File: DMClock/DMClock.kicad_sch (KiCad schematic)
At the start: 4 parts, among them J5 Conn_01x07_Pin, J6 Conn_01x07_Pin, J7 Conn_01x07_Pin, J8 Conn_01x07_Pin

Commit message: update second layer finalizations
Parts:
- removed J7, J8: Conn_01x07_Pin, Connector_PinSocket_2.54mm:PinSocket_1x07_P2.54mm_Vertical, symbol Connector:Conn_01x07_Pin
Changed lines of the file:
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@@
   (junction (at 123.6883 77.597) (diameter 0) (color 0 0 0 0)
   )
-  (junction (at 108.1415 41.402) (diameter 0) (color 0 0 0 0)
-  )
-  (junction (at 108.1415 33.782) (diameter 0) (color 0 0 0 0)
-  )
   (junction (at 109.474 61.087) (diameter 0) (color 0 0 0 0)
   )
-  (junction (at 108.1415 26.162) (diameter 0) (color 0 0 0 0)
-  )
   (junction (at 119.6963 33.782) (diameter 0) (color 0 0 0 0)
   )
-  (junction (at 108.1415 31.242) (diameter 0) (color 0 0 0 0)
-  )
   (junction (at 123.317 81.407) (diameter 0) (color 0 0 0 0)
   )
   (junction (at 119.6963 41.402) (diameter 0) (color 0 0 0 0)
   )
-  (junction (at 111.8702 28.702) (diameter 0) (color 0 0 0 0)
-  )
-  (junction (at 111.8702 31.242) (diameter 0) (color 0 0 0 0)
-  )
-  (junction (at 111.8702 36.322) (diameter 0) (color 0 0 0 0)
-  )
   (junction (at 125.349 79.502) (diameter 0) (color 0 0 0 0)
   )
   (junction (at 119.6963 26.162) (diameter 0) (color 0 0 0 0)
   )
-  (junction (at 108.1415 36.322) (diameter 0) (color 0 0 0 0)
-  )
-  (junction (at 111.8702 41.402) (diameter 0) (color 0 0 0 0)
-  )
   (junction (at 119.6963 28.702) (diameter 0) (color 0 0 0 0)
   )
   (junction (at 119.6963 38.862) (diameter 0) (color 0 0 0 0)
   )
-  (junction (at 108.1415 38.862) (diameter 0) (color 0 0 0 0)
-  )
   (junction (at 119.6963 31.242) (diameter 0) (color 0 0 0 0)
   )
   (junction (at 99.695 54.737) (diameter 0) (color 0 0 0 0)
   )
-  (junction (at 111.8702 33.782) (diameter 0) (color 0 0 0 0)
-  )
-  (junction (at 108.1415 28.702) (diameter 0) (color 0 0 0 0)
-  )
-  (junction (at 111.8702 26.162) (diameter 0) (color 0 0 0 0)
-  )
-  (junction (at 111.8702 38.862) (diameter 0) (color 0 0 0 0)
-  )
   (junction (at 106.807 49.53) (diameter 0) (color 0 0 0 0)
   )
@@
     (stroke (width 0) (type default))
   )
-  (wire (pts (xy 108.1415 26.162) (xy 111.8702 26.162))
-    (stroke (width 0) (type default))
-  )
   (wire (pts (xy 125.349 79.502) (xy 125.349 119.126))
     (stroke (width 0) (type default))
@@
     (stroke (width 0) (type default))
   )
-  (wire (pts (xy 106.807 41.402) (xy 108.1415 41.402))
-    (stroke (width 0) (type default))
-  )
   (wire (pts (xy 120.777 81.407) (xy 123.317 81.407))
     (stroke (width 0) (type default))
@@
     (stroke (width 0) (type default))
   )
-  (wire (pts (xy 111.8702 26.162) (xy 119.6963 26.162))
+  (wire (pts (xy 52.578 26.162) (xy 119.6963 26.162))
     (stroke (width 0) (type default))
   )
@@
     (stroke (width 0) (type default))
   )
-  (wire (pts (xy 52.578 26.162) (xy 108.1415 26.162))
-    (stroke (width 0) (type default))
-  )
-  (wire (pts (xy 111.8702 28.702) (xy 119.6963 28.702))
-    (stroke (width 0) (type default))
-  )
-  (wire (pts (xy 111.8702 31.242) (xy 119.6963 31.242))
-    (stroke (width 0) (type default))
-  )
-  (wire (pts (xy 99.695 33.782) (xy 108.1415 33.782))
+  (wire (pts (xy 99.695 33.782) (xy 119.6963 33.782))
     (stroke (width 0) (type default))
   )
@@
     (stroke (width 0) (type default))
   )
-  (wire (pts (xy 111.8702 38.862) (xy 119.6963 38.862))
-    (stroke (width 0) (type default))
-  )
   (wire (pts (xy 99.695 54.737) (xy 116.586 54.737))
     (stroke (width 0) (type default))
@@
     (stroke (width 0) (type default))
   )
-  (wire (pts (xy 108.1415 38.862) (xy 111.8702 38.862))
+  (wire (pts (xy 103.505 38.862) (xy 119.6963 38.862))
     (stroke (width 0) (type default))
   )
@@
     (stroke (width 0) (type default))
   )
-  (wire (pts (xy 108.1415 36.322) (xy 107.188 36.322))
-    (stroke (width 0) (type default))
-  )
   (wire (pts (xy 106.807 41.402) (xy 106.807 49.53))
     (stroke (width 0) (type default))
   )
-  (wire (pts (xy 108.1415 31.242) (xy 111.8702 31.242))
+  (wire (pts (xy 101.346 31.242) (xy 119.6963 31.242))
     (stroke (width 0) (type default))
   )
@@
     (stroke (width 0) (type default))
   )
-  (wire (pts (xy 60.198 28.702) (xy 108.1415 28.702))
+  (wire (pts (xy 60.198 28.702) (xy 119.6963 28.702))
     (stroke (width 0) (type default))
   )
@@
     (stroke (width 0) (type default))
   )
-  (wire (pts (xy 119.6963 36.322) (xy 111.8702 36.322))
-    (stroke (width 0) (type default))
-  )
   (wire (pts (xy 116.586 49.53) (xy 116.586 49.276))
     (stroke (width 0) (type default))
@@
     (stroke (width 0) (type default))
   )
-  (wire (pts (xy 108.1415 28.702) (xy 111.8702 28.702))
-    (stroke (width 0) (type default))
-  )
   (wire (pts (xy 106.807 49.53) (xy 116.586 49.53))
     (stroke (width 0) (type default))
   )
-  (wire (pts (xy 111.8702 36.322) (xy 108.1415 36.322))
+  (wire (pts (xy 107.188 36.322) (xy 119.6963 36.322))
     (stroke (width 0) (type default))
   )
@@
     (stroke (width 0) (type default))
   )
-  (wire (pts (xy 108.1415 41.402) (xy 111.8702 41.402))
+  (wire (pts (xy 106.807 41.402) (xy 119.6963 41.402))
     (stroke (width 0) (type default))
   )
@@
     (stroke (width 0) (type default))
   )
-  (wire (pts (xy 101.346 31.242) (xy 108.1415 31.242))
-    (stroke (width 0) (type default))
-  )
-  (wire (pts (xy 108.1415 33.782) (xy 111.8702 33.782))
-    (stroke (width 0) (type default))
-  )
   (wire (pts (xy 134.366 79.502) (xy 125.349 79.502))
     (stroke (width 0) (type default))
   )
-  (wire (pts (xy 111.8702 33.782) (xy 119.6963 33.782))
-    (stroke (width 0) (type default))
-  )
   (wire (pts (xy 109.474 60.96) (xy 109.474 61.087))
     (stroke (width 0) (type default))
   )
-  (wire (pts (xy 111.8702 41.402) (xy 119.6963 41.402))
-    (stroke (width 0) (type default))
-  )
   (wire (pts (xy 99.695 54.737) (xy 99.695 33.782))
     (stroke (width 0) (type default))
@@
     (stroke (width 0) (type default))
   )
-  (wire (pts (xy 103.505 38.862) (xy 108.1415 38.862))
-    (stroke (width 0) (type default))
-  )
   (wire (pts (xy 103.505 60.96) (xy 103.505 38.862))
     (stroke (width 0) (type default))
@@
   (wire (pts (xy 119.6963 26.162) (xy 129.54 26.162))
     (stroke (width 0) (type default))
-  )
-  (symbol (lib_id "Connector:Conn_01x07_Pin") (at 113.2215 33.782 180) (unit 1)
-    (in_bom yes) (on_board yes) (dnp no) (fields_autoplaced)
-    (property "Reference" "J8" (at 114.1105 32.512 0)
-      (effects (font (size 1.27 1.27)) (justify right))
-    )
-    (property "Value" "Conn_01x07_Pin" (at 114.1105 35.052 0)
-      (effects (font (size 1.27 1.27)) (justify right))
-    )
-    (property "Footprint" "Connector_PinSocket_2.54mm:PinSocket_1x07_P2.54mm_Vertical" (at 113.2215 33.782 0)
-      (effects (font (size 1.27 1.27)) hide)
-    )
-    (property "Datasheet" "~" (at 113.2215 33.782 0)
-      (effects (font (size 1.27 1.27)) hide)
-    )
-    (pin "7")
-    (pin "3")
-    (pin "1")
-    (pin "2")
-    (pin "4")
-    (pin "5")
-    (pin "6")
-    (instances
-      (project "DMClock"
-        (path "/b42b345f-a3f2-4eff-9109-2f4619119d33"
-          (reference "J8") (unit 1)
-        )
-      )
-    )
   )
   (symbol (lib_id "Connector:Conn_01x07_Pin") (at 134.62 33.782 180) (unit 1)
@@
         )
       )
-    )
-  )
-  (symbol (lib_id "Connector:Conn_01x07_Pin") (at 116.9502 33.782 180) (unit 1)
-    (in_bom yes) (on_board yes) (dnp no) (fields_autoplaced)
-    (property "Reference" "J7" (at 117.8392 32.512 0)
-      (effects (font (size 1.27 1.27)) (justify right))
-    )
-    (property "Value" "Conn_01x07_Pin" (at 117.8392 35.052 0)
-      (effects (font (size 1.27 1.27)) (justify right))
-    )
-    (property "Footprint" "Connector_PinSocket_2.54mm:PinSocket_1x07_P2.54mm_Vertical" (at 116.9502 33.782 0)
-      (effects (font (size 1.27 1.27)) hide)
-    )
-    (property "Datasheet" "~" (at 116.9502 33.782 0)
-      (effects (font (size 1.27 1.27)) hide)
-    )
-    (pin "7")
-    (pin "3")
-    (pin "1")
-    (pin "2")
-    (pin "4")
-    (pin "5")
-    (pin "6")
-    (instances
-      (project "DMClock"
-        (path "/b42b345f-a3f2-4eff-9109-2f4619119d33"
-          (reference "J7") (unit 1)
-        )
-      )

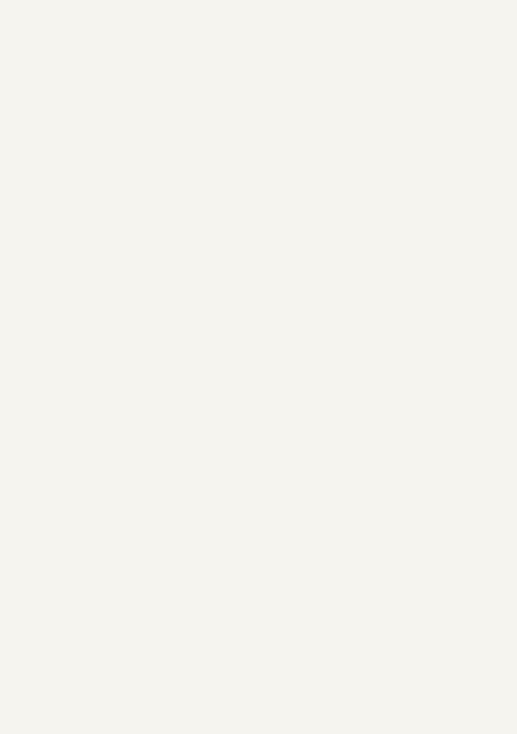
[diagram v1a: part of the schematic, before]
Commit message: finished second layer. need to finalize both first and second (double checking everything looks right, double check pwm pins, add ground plane, and finally send to pcbway. im kinda slow but hopefully done with first version pcb by tomorrow.
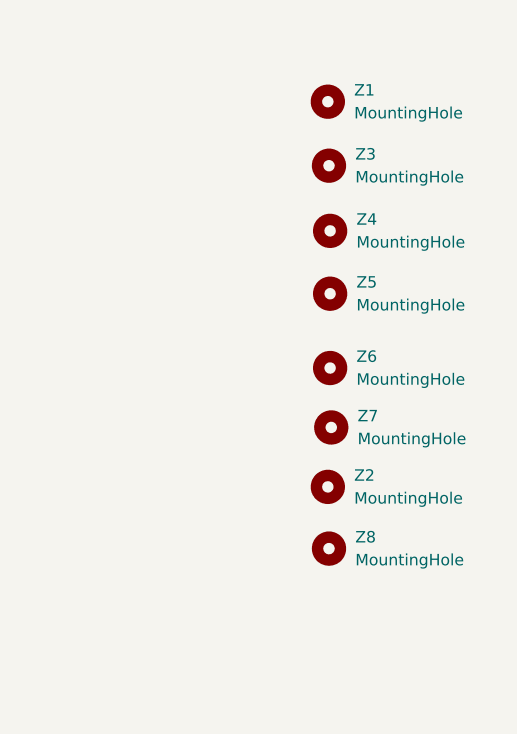
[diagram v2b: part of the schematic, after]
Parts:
- added Z1, Z2, Z3, Z4, Z5, Z6, Z7, Z8: MountingHole, MountingHole:MountingHole_2.2mm_M2, symbol Mechanical:MountingHole
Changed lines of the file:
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@@
     (stroke (width 0) (type default))
+  )
+  (symbol (lib_id "Mechanical:MountingHole") (at 222.758 40.259 0) (unit 1)
+    (in_bom yes) (on_board yes) (dnp no)
+    (property "Reference" "Z3" (at 225.679 38.989 0)
+      (effects (font (size 1.27 1.27)) (justify left))
+    )
+    (property "Value" "MountingHole" (at 225.679 41.529 0)
+      (effects (font (size 1.27 1.27)) (justify left))
+    )
+    (property "Footprint" "MountingHole:MountingHole_2.2mm_M2" (at 222.758 40.259 0)
+      (effects (font (size 1.27 1.27)) hide)
+    )
+    (property "Datasheet" "~" (at 222.758 40.259 0)
+      (effects (font (size 1.27 1.27)) hide)
+    )
+    (instances
+      (project "DMClock"
+        (path "/b42b345f-a3f2-4eff-9109-2f4619119d33"
+          (reference "Z3") (unit 1)
+        )
+      )
+    )
+  )
+  (symbol (lib_id "Mechanical:MountingHole") (at 222.885 47.498 0) (unit 1)
+    (in_bom yes) (on_board yes) (dnp no)
+    (property "Reference" "Z4" (at 225.806 46.228 0)
+      (effects (font (size 1.27 1.27)) (justify left))
+    )
+    (property "Value" "MountingHole" (at 225.806 48.768 0)
+      (effects (font (size 1.27 1.27)) (justify left))
+    )
+    (property "Footprint" "MountingHole:MountingHole_2.2mm_M2" (at 222.885 47.498 0)
+      (effects (font (size 1.27 1.27)) hide)
+    )
+    (property "Datasheet" "~" (at 222.885 47.498 0)
+      (effects (font (size 1.27 1.27)) hide)
+    )
+    (instances
+      (project "DMClock"
+        (path "/b42b345f-a3f2-4eff-9109-2f4619119d33"
+          (reference "Z4") (unit 1)
+        )
+      )
+    )
+  )
+  (symbol (lib_id "Mechanical:MountingHole") (at 222.885 54.483 0) (unit 1)
+    (in_bom yes) (on_board yes) (dnp no)
+    (property "Reference" "Z5" (at 225.806 53.213 0)
+      (effects (font (size 1.27 1.27)) (justify left))
+    )
+    (property "Value" "MountingHole" (at 225.806 55.753 0)
+      (effects (font (size 1.27 1.27)) (justify left))
+    )
+    (property "Footprint" "MountingHole:MountingHole_2.2mm_M2" (at 222.885 54.483 0)
+      (effects (font (size 1.27 1.27)) hide)
+    )
+    (property "Datasheet" "~" (at 222.885 54.483 0)
+      (effects (font (size 1.27 1.27)) hide)
+    )
+    (instances
+      (project "DMClock"
+        (path "/b42b345f-a3f2-4eff-9109-2f4619119d33"
+          (reference "Z5") (unit 1)
+        )
+      )
+    )
   )
   (symbol (lib_id "Connector:Conn_01x07_Pin") (at 134.62 33.782 180) (unit 1)
@@
     )
   )
+  (symbol (lib_id "Mechanical:MountingHole") (at 223.012 69.342 0) (unit 1)
+    (in_bom yes) (on_board yes) (dnp no)
+    (property "Reference" "Z7" (at 225.933 68.072 0)
+      (effects (font (size 1.27 1.27)) (justify left))
+    )
+    (property "Value" "MountingHole" (at 225.933 70.612 0)
+      (effects (font (size 1.27 1.27)) (justify left))
+    )
+    (property "Footprint" "MountingHole:MountingHole_2.2mm_M2" (at 223.012 69.342 0)
+      (effects (font (size 1.27 1.27)) hide)
+    )
+    (property "Datasheet" "~" (at 223.012 69.342 0)
+      (effects (font (size 1.27 1.27)) hide)
+    )
+    (instances
+      (project "DMClock"
+        (path "/b42b345f-a3f2-4eff-9109-2f4619119d33"
+          (reference "Z7") (unit 1)
+        )
+      )
+    )
+  )
   (symbol (lib_id "power:GND") (at 107.188 36.322 270) (unit 1)
     (in_bom yes) (on_board yes) (dnp no) (fields_autoplaced)
@@
         )
       )
+    )
+  )
+  (symbol (lib_id "Mechanical:MountingHole") (at 222.631 33.147 0) (unit 1)
+    (in_bom yes) (on_board yes) (dnp no)
+    (property "Reference" "Z1" (at 225.552 31.877 0)
+      (effects (font (size 1.27 1.27)) (justify left))
+    )
+    (property "Value" "MountingHole" (at 225.552 34.417 0)
+      (effects (font (size 1.27 1.27)) (justify left))
+    )
+    (property "Footprint" "MountingHole:MountingHole_2.2mm_M2" (at 222.631 33.147 0)
+      (effects (font (size 1.27 1.27)) hide)
+    )
+    (property "Datasheet" "~" (at 222.631 33.147 0)
+      (effects (font (size 1.27 1.27)) hide)
+    )
+    (instances
+      (project "DMClock"
+        (path "/b42b345f-a3f2-4eff-9109-2f4619119d33"
+          (reference "Z1") (unit 1)
+        )
+      )
+    )
+  )
+  (symbol (lib_id "Mechanical:MountingHole") (at 222.631 75.946 0) (unit 1)
+    (in_bom yes) (on_board yes) (dnp no)
+    (property "Reference" "Z2" (at 225.552 74.676 0)
+      (effects (font (size 1.27 1.27)) (justify left))
+    )
+    (property "Value" "MountingHole" (at 225.552 77.216 0)
+      (effects (font (size 1.27 1.27)) (justify left))
+    )
+    (property "Footprint" "MountingHole:MountingHole_2.2mm_M2" (at 222.631 75.946 0)
+      (effects (font (size 1.27 1.27)) hide)
+    )
+    (property "Datasheet" "~" (at 222.631 75.946 0)
+      (effects (font (size 1.27 1.27)) hide)
+    )
+    (instances
+      (project "DMClock"
+        (path "/b42b345f-a3f2-4eff-9109-2f4619119d33"
+          (reference "Z2") (unit 1)
+        )
+      )
+    )
+  )
+  (symbol (lib_id "Mechanical:MountingHole") (at 222.885 62.738 0) (unit 1)
+    (in_bom yes) (on_board yes) (dnp no)
+    (property "Reference" "Z6" (at 225.806 61.468 0)
+      (effects (font (size 1.27 1.27)) (justify left))
+    )
+    (property "Value" "MountingHole" (at 225.806 64.008 0)
+      (effects (font (size 1.27 1.27)) (justify left))
+    )
+    (property "Footprint" "MountingHole:MountingHole_2.2mm_M2" (at 222.885 62.738 0)
+      (effects (font (size 1.27 1.27)) hide)
+    )
+    (property "Datasheet" "~" (at 222.885 62.738 0)
+      (effects (font (size 1.27 1.27)) hide)
+    )
+    (instances
+      (project "DMClock"
+        (path "/b42b345f-a3f2-4eff-9109-2f4619119d33"
+          (reference "Z6") (unit 1)
+        )
+      )
+    )
+  )
+  (symbol (lib_id "Mechanical:MountingHole") (at 222.758 82.804 0) (unit 1)
+    (in_bom yes) (on_board yes) (dnp no)
+    (property "Reference" "Z8" (at 225.679 81.534 0)
+      (effects (font (size 1.27 1.27)) (justify left))
+    )
+    (property "Value" "MountingHole" (at 225.679 84.074 0)
+      (effects (font (size 1.27 1.27)) (justify left))
+    )
+    (property "Footprint" "MountingHole:MountingHole_2.2mm_M2" (at 222.758 82.804 0)
+      (effects (font (size 1.27 1.27)) hide)
+    )
+    (property "Datasheet" "~" (at 222.758 82.804 0)
+      (effects (font (size 1.27 1.27)) hide)
+    )
+    (instances
+      (project "DMClock"
+        (path "/b42b345f-a3f2-4eff-9109-2f4619119d33"
+          (reference "Z8") (unit 1)
+        )
+      )
